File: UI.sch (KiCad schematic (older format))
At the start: 42 parts, among them Q1 2N7002BK, Q2 BS250P, U3 TXB0104, U7 TXB0108

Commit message: Update UI.sch
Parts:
- added U? (x2): TLV2333IDR, Package_SO:SOIC-8_3.9x4.9mm_P1.27mm, symbol OpenVent:TLV2333IDR
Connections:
- net labels added: +3.3V
- wire segments 237 -> 251
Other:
- moved on the sheet: D15A, D15B, JP2, LS1, LS2, Q1, Q2, R35, R36, R49, R88, R89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

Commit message: Update UI.sch
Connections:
- net labels added: PB_MUTE_FPGA, PB_MUTE_MCU
- wire segments 251 -> 254
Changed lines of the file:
@@
 	6600 3150 6600 3050
 Wire Wire Line
-	7000 2650 7000 1850
+	7000 2650 7000 2200
 Wire Wire Line
 	7000 1850 6050 1850
@@
 	5650 2750 5900 2750
 Connection ~ 5900 2750
+Text GLabel 7300 2200 2    50   Output ~ 0
+PB_MUTE_MCU
+Wire Wire Line
+	7300 2200 7000 2200
+Connection ~ 7000 2200
+Wire Wire Line
+	7000 2200 7000 1850
+Text GLabel 7300 3900 2    50   Output ~ 0
+PB_MUTE_FPGA
+Wire Wire Line
+	7300 3900 7100 3900
+Connection ~ 7100 3900
 $EndSCHEMATC

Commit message: Update LED RGB serial to part to BB-HRGB32M-TRB-C
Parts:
- removed D10, D11, D4, D5, D6, D7, D8, D9: BB-HRGB32M-TRB, OpenVent:LED_RGB_BL-RRGB32M_TRB_PLCC4_3.2x2.8mm, symbol OpenVent:LED_RGB_Serial
- added D10, D11, D4, D5, D6, D7, D8, D9: BB-HRGB32M-TRB-C, symbol OpenVent:BB-HRGB32M-TRB-C

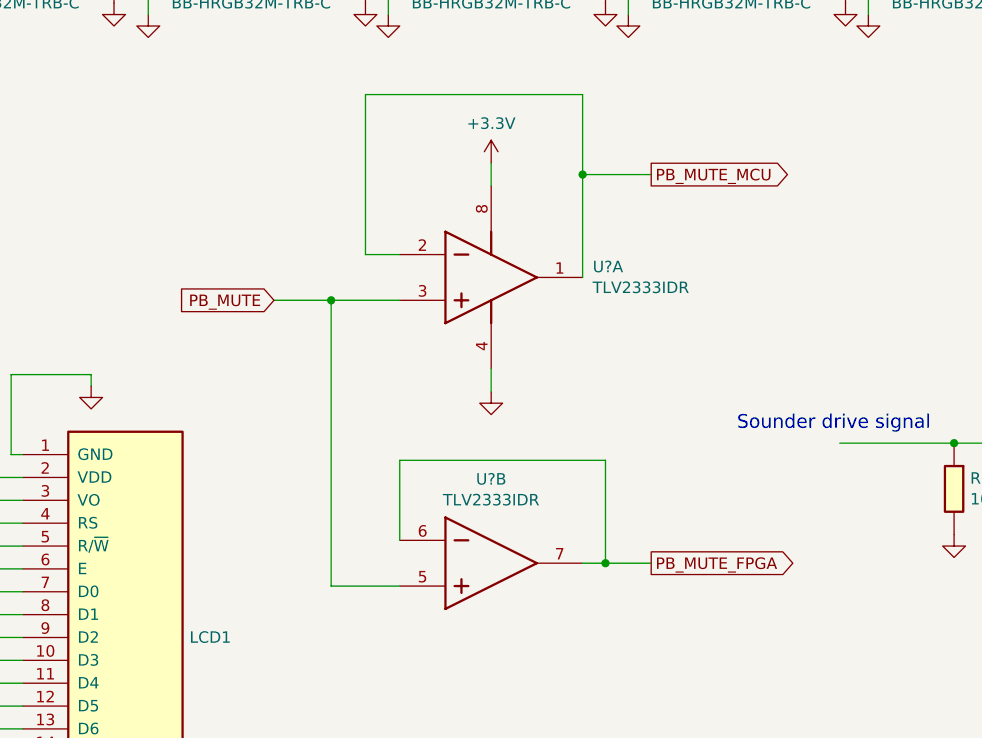
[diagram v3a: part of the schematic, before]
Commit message: Update UI.sch
BUFFER SIGNALS CHANGED FOR PB_SEL
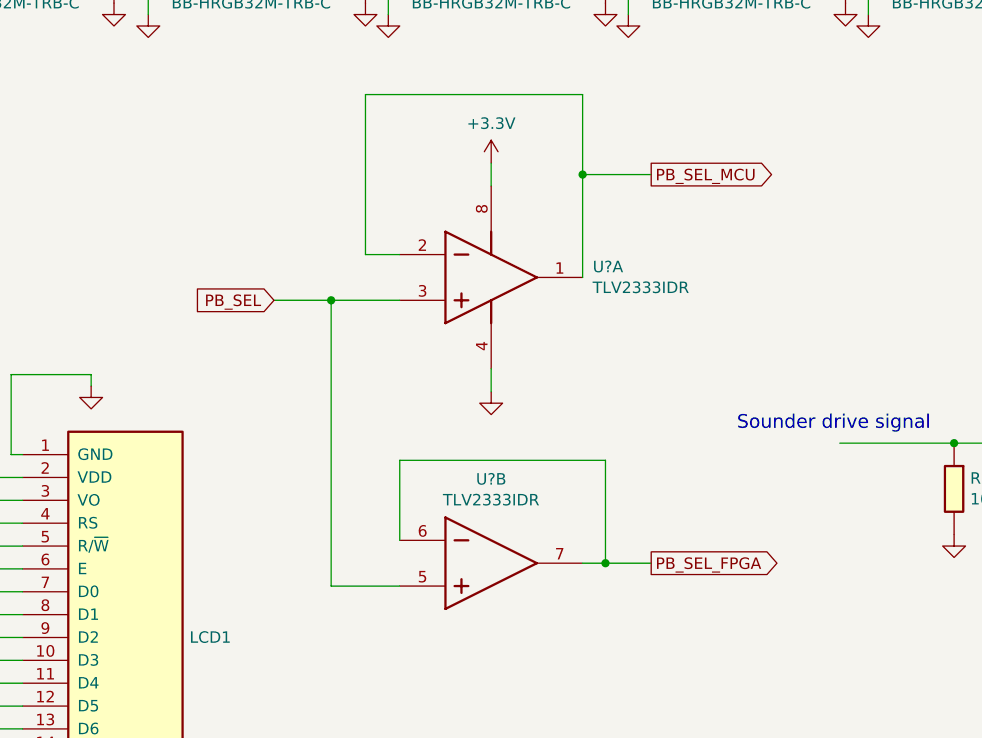
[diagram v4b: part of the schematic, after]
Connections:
- net PB_MUTE: no longer U?.3 (INA+), U?.5 (INB+)
- net PB_SEL: now also U?.3 (INA+), U?.5 (INB+)
- net PB_MUTE_FPGA renamed PB_SEL_FPGA
- net PB_MUTE_MCU renamed PB_SEL_MCU
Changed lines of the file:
@@
 $Descr A4 11693 8268
 encoding utf-8
-Sheet 8 9
+Sheet 7 9
 Title ""
 Date ""
@@
 	5900 2750 6200 2750
 Text GLabel 5650 2750 0    50   Input ~ 0
-PB_MUTE
+PB_SEL
 Wire Wire Line
 	5650 2750 5900 2750
 Connection ~ 5900 2750
 Text GLabel 7300 2200 2    50   Output ~ 0
-PB_MUTE_MCU
+PB_SEL_MCU
 Wire Wire Line
 	7300 2200 7000 2200
@@
 	7000 2200 7000 1850
 Text GLabel 7300 3900 2    50   Output ~ 0
-PB_MUTE_FPGA
+PB_SEL_FPGA
 Wire Wire Line
 	7300 3900 7100 3900

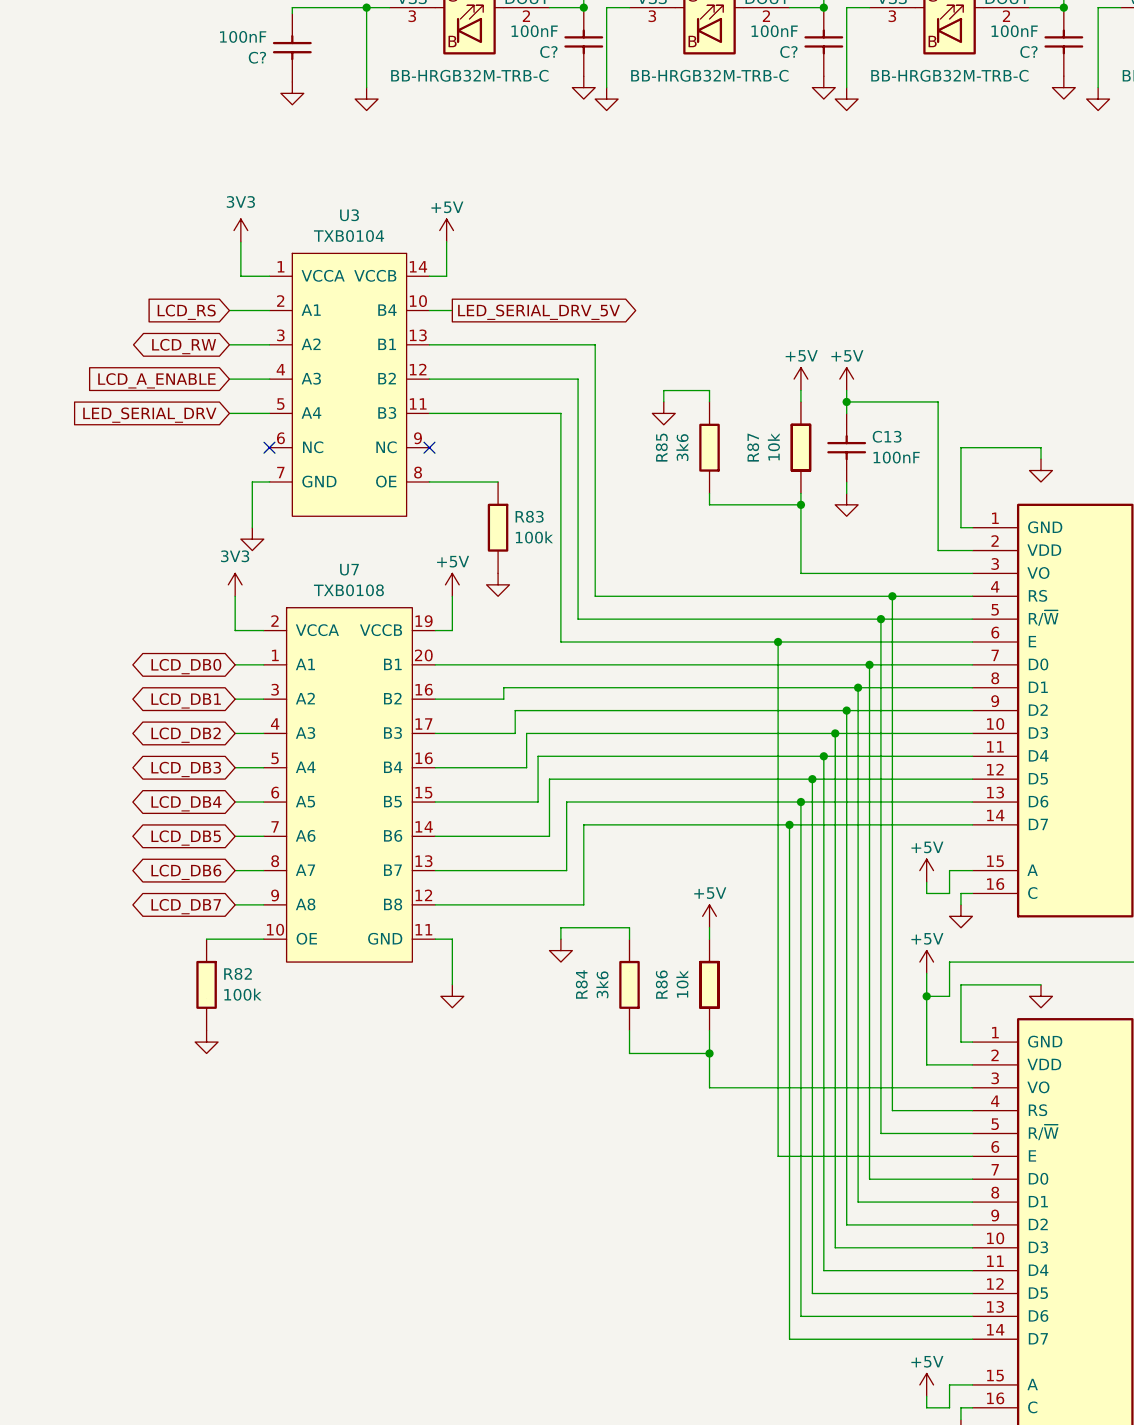
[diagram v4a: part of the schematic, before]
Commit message: LCD Enable lines have been separated
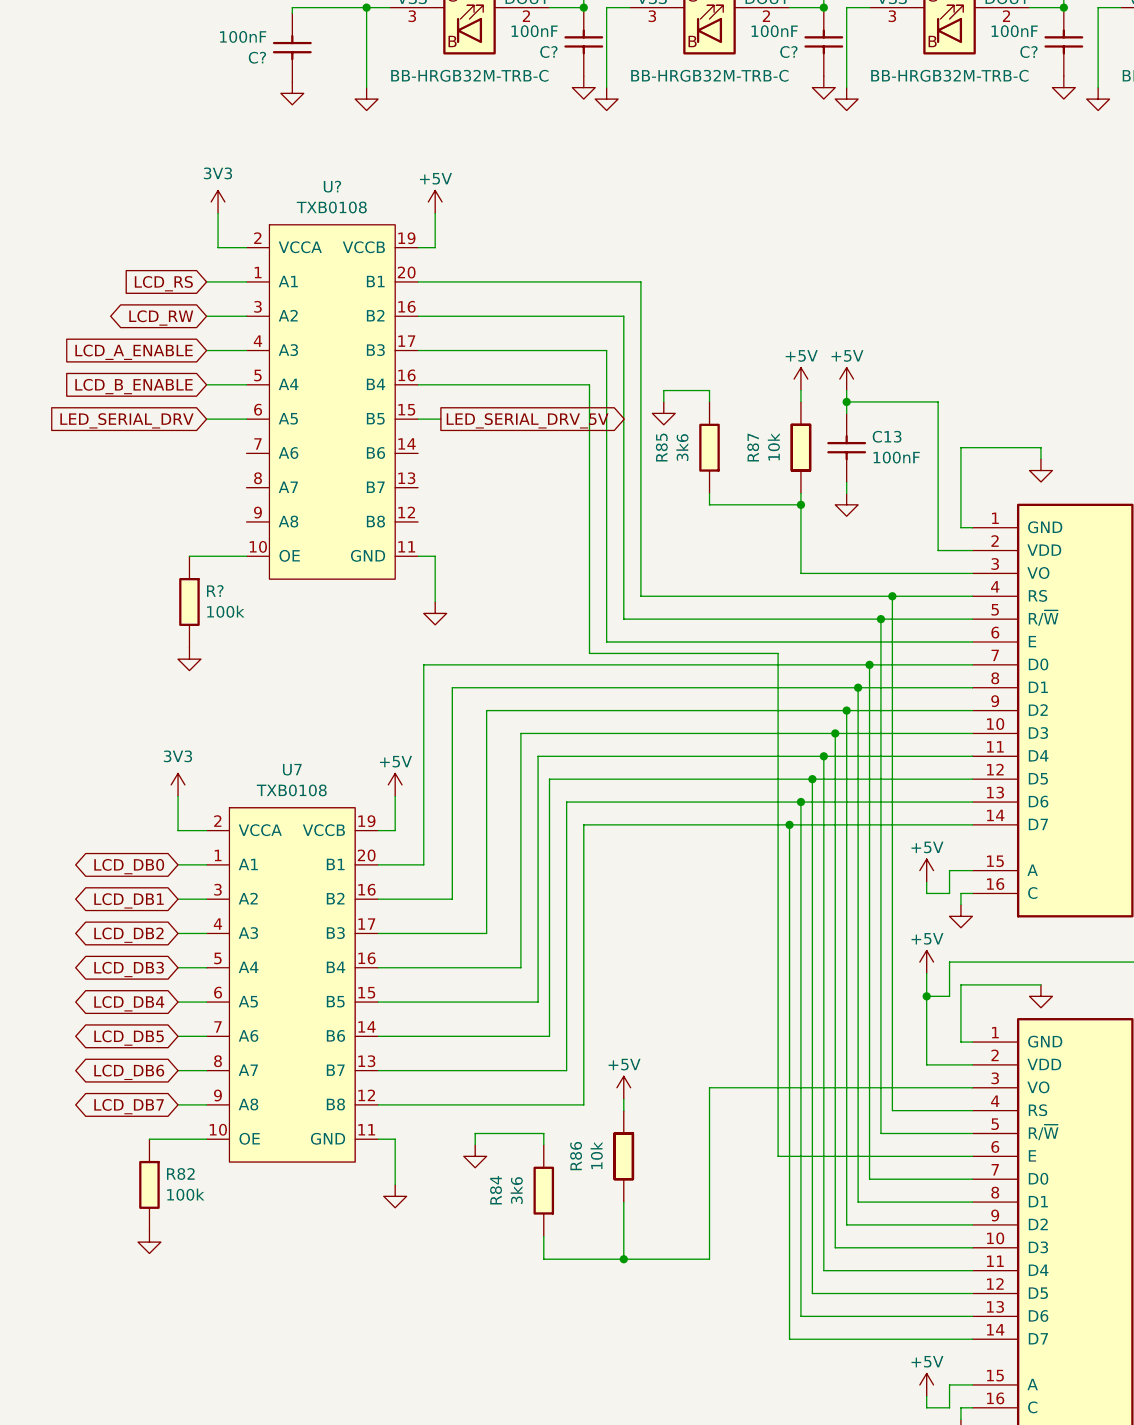
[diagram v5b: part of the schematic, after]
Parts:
- removed R83: 100K_0603_Chip_Resistor,_1%,_0.1W, symbol OpenVent:100K_0603_Chip_Resistor,_1%,_0.1W
- removed U3: TXB0104, symbol OpenVent:TXB0104
- added R?: 100K_0603_Chip_Resistor,_1%,_0.1W, symbol OpenVent:100K_0603_Chip_Resistor,_1%,_0.1W
- added U?: TXB0108, symbol OpenVent:TXB0108
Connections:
- net +3V3: now also U?.2 (VCCA)
- net +5V: now also U?.19 (VCCB)
- net GND: now also R?.2, U?.11 (GND)
- net LCD_A_ENABLE: now also U?.4 (A3)
- net LCD_RS: now also U?.1 (A1)
- net LCD_RW: now also U?.3 (A2)
- net LED_SERIAL_DRV: now also U?.6 (A5)
- net LED_SERIAL_DRV_5V: now also U?.15 (B5)
- net at LCD1.4 (RS), LCD2.4 (RS): now also U?.20 (B1)
- net at LCD1.5 (R/~W), LCD2.5 (R/~W): now also U?.16 (B4)
- net at LCD1.6 (E): now also U?.17 (B3); no longer LCD2.6 (E)
- new net: LCD2.6 (E), U?.16 (B4)
- new net: R?.1, U?.10 (OE)
- new net LCD_B_ENABLE: U?.5 (A4)
- no-connect marks 2 -> 0
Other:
- moved on the sheet: R82, R84, R86, U7

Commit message: Update UI.sch
Pull up / Cap to UI and buffer inverter added
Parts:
- removed U? (x2): TLV2333IDR, Package_SO:SOIC-8_3.9x4.9mm_P1.27mm, symbol OpenVent:TLV2333IDR
- added C? (x4): 100nF_0603_Ceramic_Capacitor,_10%,_X7R,_25V, symbol OpenVent:100nF_0603_Ceramic_Capacitor,_10%,_X7R,_25V
- added IC?: SN74LVC2G14DBVR, SOT95P280X145-6N, symbol OpenVent:SN74LVC2G14DBVR
- added R? (x6): 47k_0603_Chip_Resistor,_1%,_0.1W, symbol OpenVent:47k_0603_Chip_Resistor,_1%,_0.1W
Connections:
- net labels added: +3V3-ALWAYS-ON
- wire segments 260 -> 301
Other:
- note added: "Membrane \nPush Button \nConnector"
- note removed: "Membrane Push Button Connector"
- moved on the sheet: D15A, D15B, D16A, D16B, JP2, R88, R89, R90, R91

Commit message: Update UI.sch
keypad buffer replaced
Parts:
- removed IC?: SN74LVC2G14DBVR, SOT95P280X145-6N, symbol OpenVent:SN74LVC2G14DBVR
- added IC?: SN74LVC2G14DBVR, SOT95P280X145-6N, symbol OpenVent:SN74LVC2G14DBVR
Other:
- moved on the sheet: R?
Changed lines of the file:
@@
 	1    0    0    -1
 $EndComp
-Text GLabel 5450 2650 0    50   Input ~ 0
+Text GLabel 5450 2700 0    50   Input ~ 0
 PB_SEL
-Text GLabel 7750 2850 2    50   Output ~ 0
+Text GLabel 7650 2800 2    50   Output ~ 0
 PB_SEL_MCU
-Text GLabel 6750 2100 0    50   Output ~ 0
+Text GLabel 7650 2600 2    50   Output ~ 0
 PB_SEL_FPGA
 $Comp
@@
 L OpenVent:+3V3-ALWAYS-ON #PWR?
 U 1 1 607599E9
-P 7600 2050
-F 0 "#PWR?" H 7600 1950 50  0001 C CNN
-F 1 "+3V3-ALWAYS-ON" H 7600 2223 50  0000 C CNN
-F 2 "" H 7600 2050 50  0001 C CNN
-F 3 "" H 7600 2050 50  0001 C CNN
-	1    7600 2050
-	1    0    0    -1
-$EndComp
-Wire Wire Line
-	7600 2750 6950 2750
+P 7000 2150
+F 0 "#PWR?" H 7000 2050 50  0001 C CNN
+F 1 "+3V3-ALWAYS-ON" H 7000 2323 50  0000 C CNN
+F 2 "" H 7000 2150 50  0001 C CNN
+F 3 "" H 7000 2150 50  0001 C CNN
+	1    7000 2150
+	1    0    0    -1
+$EndComp
 $Comp
 L OpenVent:47k_0603_Chip_Resistor,_1%,_0.1W R?
 U 1 1 607725C7
-P 7200 2950
-F 0 "R?" H 7300 3057 50  0000 C CNN
-F 1 "47k_0603_Chip_Resistor,_1%,_0.1W" H 7200 2950 50  0001 C CNN
-F 2 "" H 7200 2950 50  0001 C CNN
-F 3 "" H 7200 2950 50  0001 C CNN
-F 4 "47k" H 7300 2966 50  0000 C CNN "Val"
-F 5 "1%" H 7200 2950 50  0001 C CNN "Tolerance"
-F 6 "0.1W" H 7200 2950 50  0001 C CNN "Watt"
-	1    7200 2950
+P 7150 2900
+F 0 "R?" H 7250 3007 50  0000 C CNN
+F 1 "47k_0603_Chip_Resistor,_1%,_0.1W" H 7150 2900 50  0001 C CNN
+F 2 "" H 7150 2900 50  0001 C CNN
+F 3 "" H 7150 2900 50  0001 C CNN
+F 4 "47k" H 7250 2916 50  0000 C CNN "Val"
+F 5 "1%" H 7150 2900 50  0001 C CNN "Tolerance"
+F 6 "0.1W" H 7150 2900 50  0001 C CNN "Watt"
+	1    7150 2900
 	1    0    0    1
 $EndComp
@@
 L OpenVent:47k_0603_Chip_Resistor,_1%,_0.1W R?
 U 1 1 60774C7C
-P 7150 2250
-F 0 "R?" V 7204 2220 50  0000 L CNN
-F 1 "47k_0603_Chip_Resistor,_1%,_0.1W" H 7150 2250 50  0001 C CNN
-F 2 "" H 7150 2250 50  0001 C CNN
-F 3 "" H 7150 2250 50  0001 C CNN
-F 4 "47k" V 7295 2220 50  0000 L CNN "Val"
-F 5 "1%" H 7150 2250 50  0001 C CNN "Tolerance"
-F 6 "0.1W" H 7150 2250 50  0001 C CNN "Watt"
-	1    7150 2250
-	0    1    1    0
-$EndComp
-Wire Wire Line
-	6950 2850 7100 2850
-Wire Wire Line
-	6950 2650 7050 2650
-Wire Wire Line
-	7050 2650 7050 2550
-$Comp
-L OpenVent:SN74LVC2G14DBVR IC?
-U 1 1 60741737
-P 5950 2650
-F 0 "IC?" H 6450 2915 50  0000 C CNN
-F 1 "SN74LVC2G14DBVR" H 6450 2824 50  0000 C CNN
-F 2 "SOT95P280X145-6N" H 6800 2750 50  0001 L CNN
-F 3 "http://componentsearchengine.com/Datasheets/3/SN74LVC2G14DBVR.pdf" H 6800 2650 50  0001 L CNN
-F 4 "DUAL SCHMITT-TRIGGER INVERTER" H 6800 2550 50  0001 L CNN "Description"
-F 5 "1.45" H 6800 2450 50  0001 L CNN "Height"
-F 6 "Texas Instruments" H 6800 2350 50  0001 L CNN "Manufacturer_Name"
-F 7 "SN74LVC2G14DBVR" H 6800 2250 50  0001 L CNN "Manufacturer_Part_Number"
-F 8 "595-SN74LVC2G14DBVR" H 6800 2150 50  0001 L CNN "Mouser Part Number"
-F 9 "https://www.mouser.co.uk/ProductDetail/Texas-Instruments/SN74LVC2G14DBVR/?qs=q2XTDbzbm6DXbZiJ8Yzjpw%3D%3D" H 6800 2050 50  0001 L CNN "Mouser Price/Stock"
-F 10 "SN74LVC2G14DBVR" H 6800 1950 50  0001 L CNN "Arrow Part Number"
-F 11 "https://www.arrow.com/en/products/sn74lvc2g14dbvr/texas-instruments" H 6800 1850 50  0001 L CNN "Arrow Price/Stock"
-	1    5950 2650
-	1    0    0    -1
-$EndComp
-Wire Wire Line
-	5950 2750 5700 2750
+P 7150 2500
+F 0 "R?" V 7204 2470 50  0000 L CNN
+F 1 "47k_0603_Chip_Resistor,_1%,_0.1W" H 7150 2500 50  0001 C CNN
+F 2 "" H 7150 2500 50  0001 C CNN
+F 3 "" H 7150 2500 50  0001 C CNN
+F 4 "47k" V 7295 2470 50  0000 L CNN "Val"
+F 5 "1%" H 7150 2500 50  0001 C CNN "Tolerance"
+F 6 "0.1W" H 7150 2500 50  0001 C CNN "Watt"
+	1    7150 2500
+	1    0    0    -1
+$EndComp
 $Comp
 L OpenVent:GND #PWR?
 U 1 1 60741EE3
-P 5700 2900
-F 0 "#PWR?" H 5700 2650 50  0001 C CNN
-F 1 "GND" H 5700 2750 50  0001 C CNN
-F 2 "" H 5700 2900 50  0001 C CNN
-F 3 "" H 5700 2900 50  0001 C CNN
-	1    5700 2900
-	1    0    0    -1
-$EndComp
-Wire Wire Line
-	5950 2850 5900 2850
-Wire Wire Line
-	5900 2850 5900 2650
-Connection ~ 5900 2650
-Wire Wire Line
-	5900 2650 5950 2650
-Wire Wire Line
-	5700 2750 5700 2900
-Wire Wire Line
-	5450 2650 5900 2650
-Wire Wire Line
-	7600 2050 7600 2750
-Wire Wire Line
-	7500 2850 7750 2850
-Wire Wire Line
-	7050 2150 7050 2100
-Wire Wire Line
-	7050 2100 6750 2100
+P 5500 2300
+F 0 "#PWR?" H 5500 2050 50  0001 C CNN
+F 1 "GND" H 5500 2150 50  0001 C CNN
+F 2 "" H 5500 2300 50  0001 C CNN
+F 3 "" H 5500 2300 50  0001 C CNN
+	1    5500 2300
+	1    0    0    -1
+$EndComp
 $Comp
 L OpenVent:100nF_0603_Ceramic_Capacitor,_10%,_X7R,_25V C?
@@
 Wire Wire Line
 	7450 6150 7650 6150
+$Comp
+L OpenVent:SN74LVC2G14DBVR IC?
+U 1 1 607790C5
+P 5800 2550
+F 0 "IC?" H 6300 2925 50  0000 C CNN
+F 1 "SN74LVC2G14DBVR" H 6300 2834 50  0000 C CNN
+F 2 "SOT95P280X145-6N" H 6650 2650 50  0001 L CNN
+F 3 "http://componentsearchengine.com/Datasheets/3/SN74LVC2G14DBVR.pdf" H 6650 2500 50  0001 L CNN
+F 4 "DUAL SCHMITT-TRIGGER INVERTER" H 6650 2400 50  0001 L CNN "Description"
+F 5 "1.45" H 6650 2300 50  0001 L CNN "Height"
+F 6 "Texas Instruments" H 6650 2250 50  0001 L CNN "Manufacturer_Name"
+F 7 "SN74LVC2G14DBVR" H 6650 2150 50  0001 L CNN "Manufacturer_Part_Number"
+F 8 "595-SN74LVC2G14DBVR" H 6650 2050 50  0001 L CNN "Mouser Part Number"
+F 9 "https://www.mouser.co.uk/ProductDetail/Texas-Instruments/SN74LVC2G14DBVR/?qs=q2XTDbzbm6DXbZiJ8Yzjpw%3D%3D" H 6650 1950 50  0001 L CNN "Mouser Price/Stock"
+F 10 "SN74LVC2G14DBVR" H 6650 1850 50  0001 L CNN "Arrow Part Number"
+F 11 "https://www.arrow.com/en/products/sn74lvc2g14dbvr/texas-instruments" H 6650 1750 50  0001 L CNN "Arrow Price/Stock"
+	1    5800 2550
+	1    0    0    -1
+$EndComp
+Wire Wire Line
+	6800 2600 7050 2600
+Wire Wire Line
+	7450 2600 7650 2600
+Wire Wire Line
+	7650 2800 7450 2800
+Wire Wire Line
+	7050 2800 6800 2800
+Wire Wire Line
+	6800 2400 7000 2400
+Wire Wire Line
+	7000 2400 7000 2150
+Wire Wire Line
+	5800 2600 5700 2600
+Wire Wire Line
+	5700 2600 5700 2700
+Wire Wire Line
+	5700 2800 5800 2800
+Connection ~ 5700 2700
+Wire Wire Line
+	5700 2700 5700 2800
+Wire Wire Line
+	5800 2400 5800 2150
+Wire Wire Line
+	5800 2150 5500 2150
+Wire Wire Line
+	5500 2150 5500 2300
+Wire Wire Line
+	5450 2700 5700 2700
 $EndSCHEMATC
